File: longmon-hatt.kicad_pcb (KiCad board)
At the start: 2 copper layers, 67 x 35 mm, 4 parts

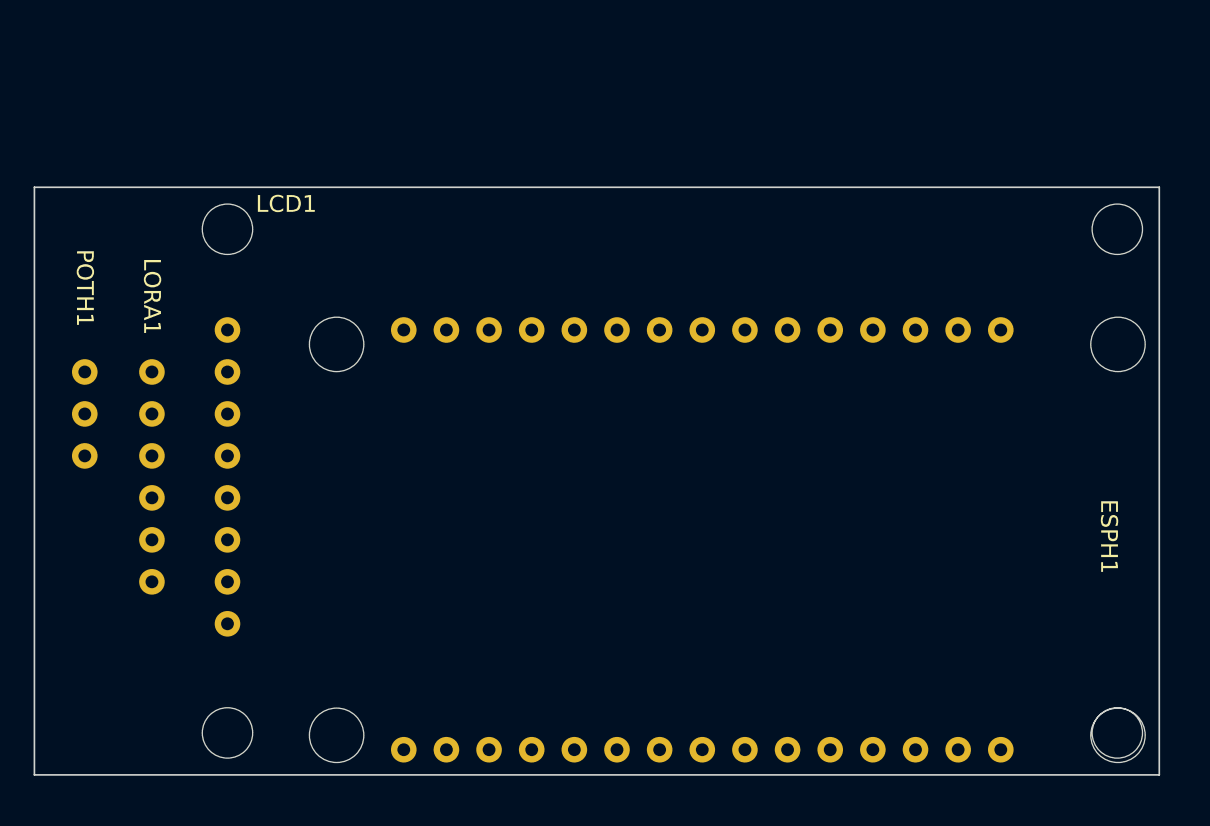
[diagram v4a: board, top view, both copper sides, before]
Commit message: Extend pcb 0.5mm down
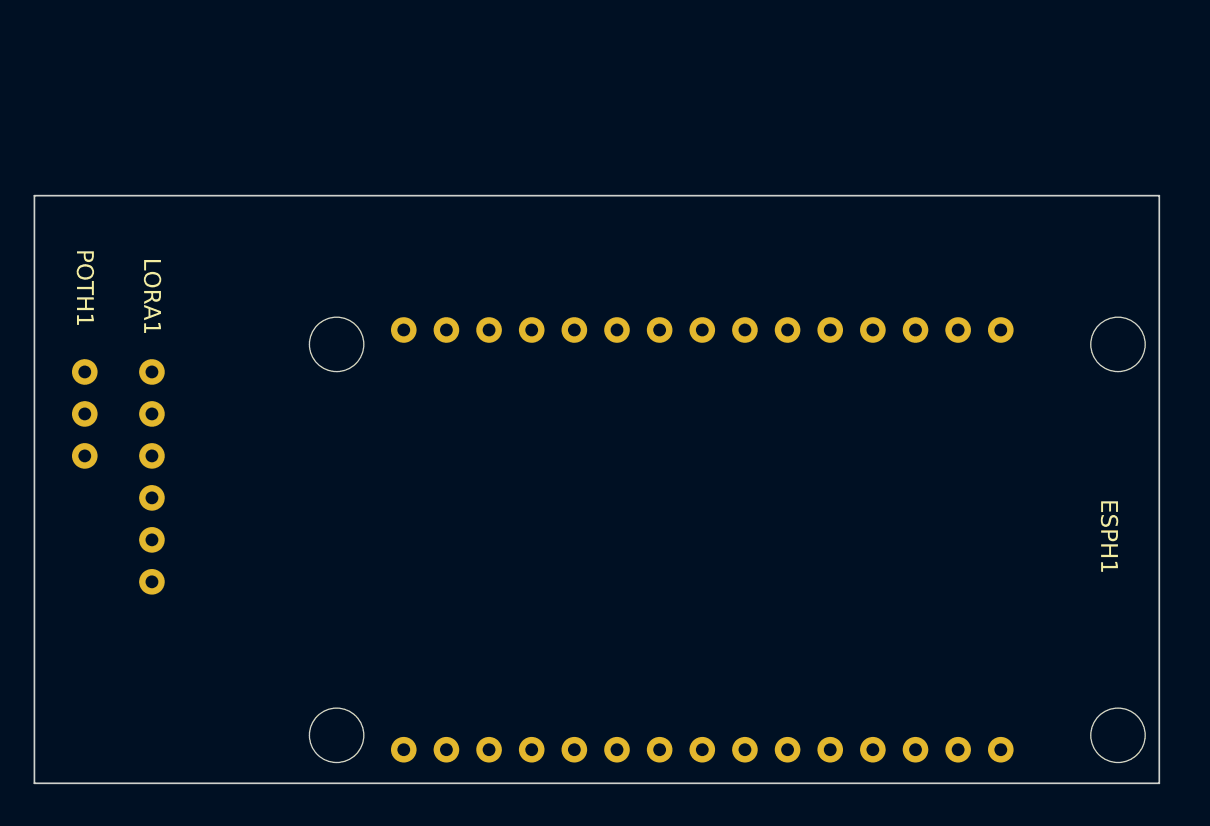
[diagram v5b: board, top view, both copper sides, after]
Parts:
- removed LCD1: ~, ESP:LCD Module

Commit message: Add LCD to PCB
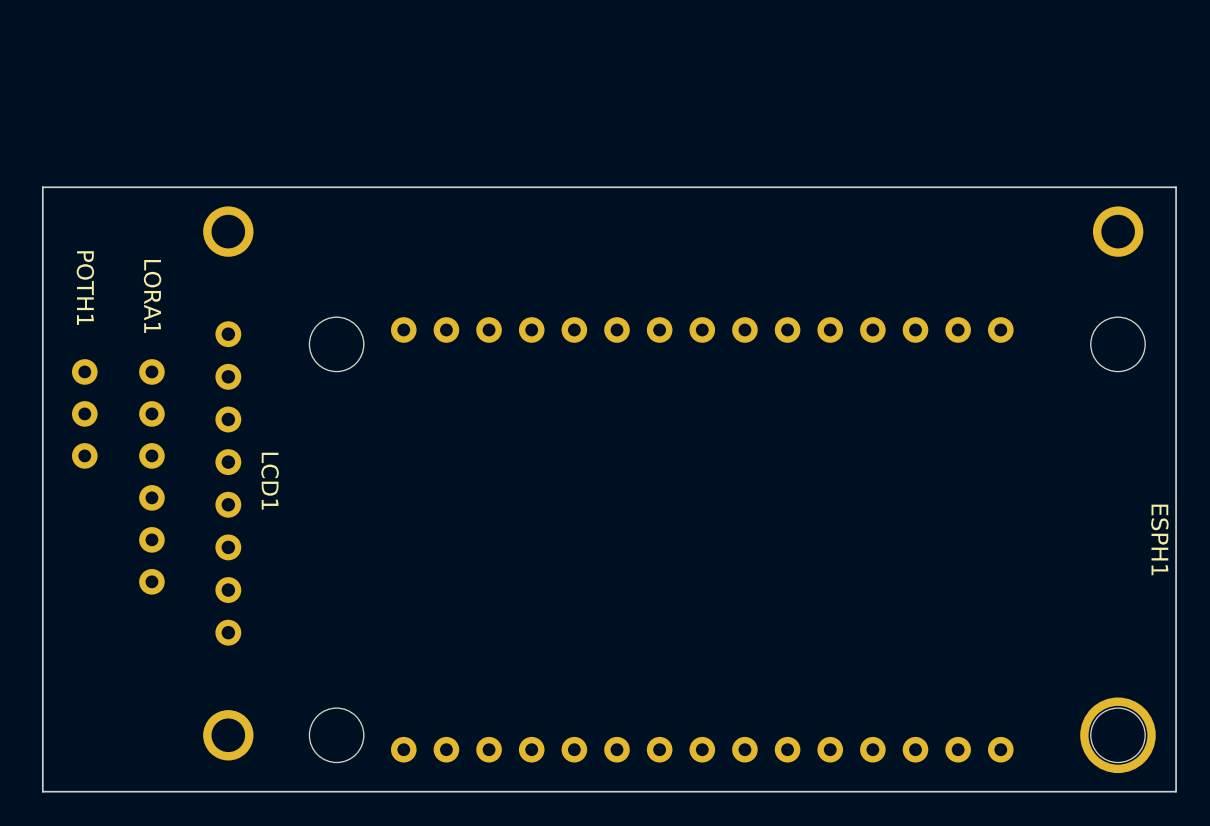
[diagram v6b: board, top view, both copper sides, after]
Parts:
- added LCD1: ~, ESP:LCD Module, F.Cu at (139.6, 81.6)
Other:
- board size 67 x 35 mm -> 67.5 x 36 mm

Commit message: Remove LCD 4th mounting hole, silkscreen thickness to 0.153mm
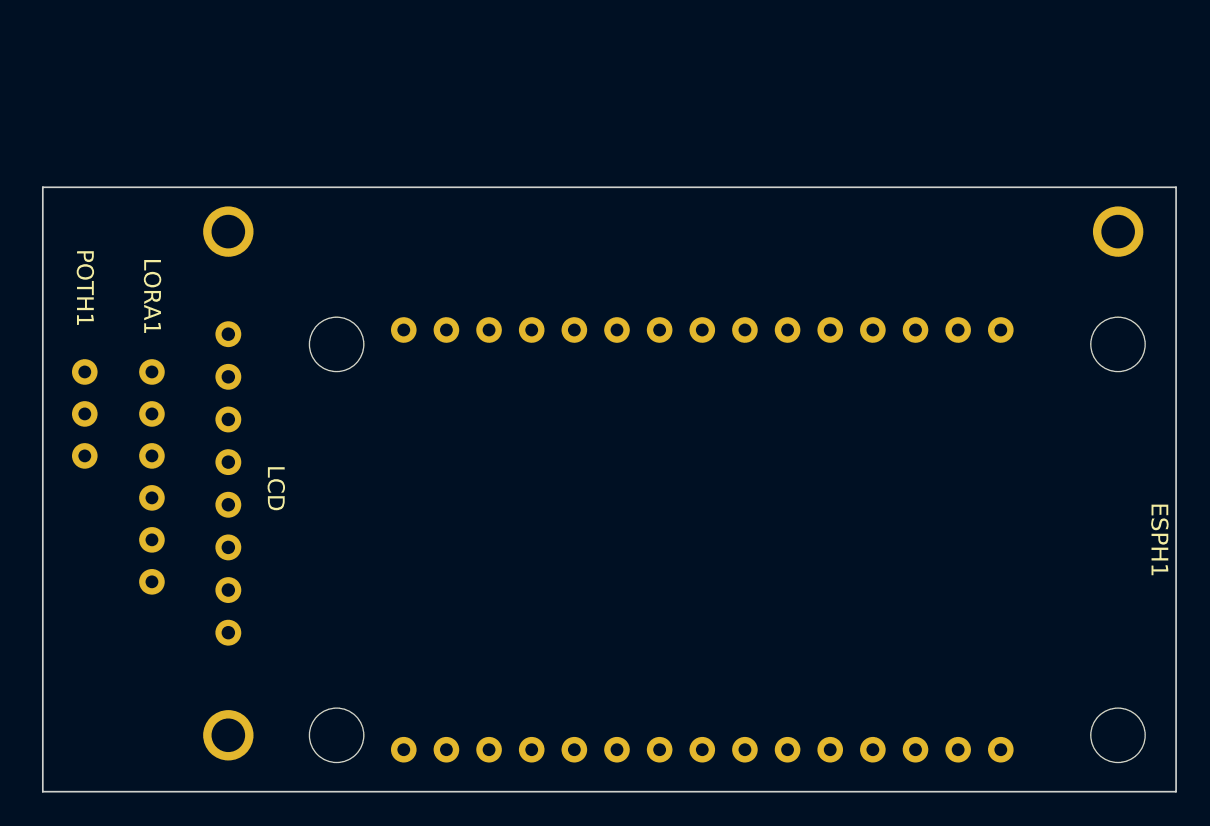
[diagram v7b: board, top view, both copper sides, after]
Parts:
- removed LCD1: ~, ESP:LCD Module
- added LCD: LCD Module, ESP:LCD Module, F.Cu at (139.6, 81.6)
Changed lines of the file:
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@@
     (attr through_hole)
     (fp_text reference "ESPH1" (at 12.5 45 270 unlocked) (layer "F.SilkS")
-        (effects (font (size 1 1) (thickness 0.1)))
+        (effects (font (size 1 1) (thickness 0.153)))
     )
     (fp_text value "~" (at 12.7 0 90 unlocked) (layer "F.Fab") hide
@@
     (property "Sim.Enable" "0")
     (attr through_hole)
-    (fp_text reference "LORA1" (at 0 -4.5 -90 unlocked) (layer "F.SilkS")
-        (effects (font (size 1 1) (thickness 0.1)))
+    (fp_text reference "LORA1" (at 0 -4.5 270 unlocked) (layer "F.SilkS")
+        (effects (font (size 1 1) (thickness 0.153)))
     )
     (fp_text value "~" (at 12.5 -5 unlocked) (layer "F.Fab") hide
@@
       (net 1 "Net-(LCD1-VCC)") (pinfunction "VDD") (pintype "power_in"))
   )
-  (footprint "ESP:POT Header" (layer "F.Cu")
-    (at 131 90)
-    (property "Sheetfile" "longmon-hatt.kicad_sch")
-    (property "Sheetname" "")
-    (property "Sim.Enable" "0")
-    (attr through_hole)
-    (fp_text reference "POTH1" (at 0 -5 -90 unlocked) (layer "F.SilkS")
-        (effects (font (size 1 1) (thickness 0.1)))
-    )
-    (fp_text value "~" (at 7.5 1.5 unlocked) (layer "F.Fab") hide
-        (effects (font (size 1 1) (thickness 0.15)))
-    )
-    (fp_text user "${REFERENCE}" (at 7.5 3 unlocked) (layer "F.Fab") hide
-        (effects (font (size 1 1) (thickness 0.15)))
-    )
-    (pad "DIV" thru_hole circle (at 0 2.5) (size 1.524 1.524) (drill 0.762) (layers "*.Cu" "*.Mask")
-      (net 5 "Net-(ESPH1-D34)") (pinfunction "DIV") (pintype "output"))
-    (pad "GND" thru_hole circle (at 0 5) (size 1.524 1.524) (drill 0.762) (layers "*.Cu" "*.Mask")
-      (net 28 "Net-(LCD1-GND)") (pinfunction "GND") (pintype "power_in"))
-    (pad "VCC" thru_hole circle (at 0 0) (size 1.524 1.524) (drill 0.762) (layers "*.Cu" "*.Mask")
-      (net 1 "Net-(LCD1-VCC)") (pinfunction "VCC") (pintype "power_in"))
-  )
   (footprint "ESP:LCD Module" (layer "F.Cu")
     (at 139.55 81.64)
-    (property "Sheetfile" "longmon-hatt.kicad_sch")
-    (property "Sheetname" "")
-    (property "Sim.Enable" "0")
     (attr through_hole)
-    (fp_text reference "LCD1" (at 2.45 14.86 -90 unlocked) (layer "F.SilkS")
-        (effects (font (size 1 1) (thickness 0.1)))
+    (fp_text reference "LCD" (at 2.82 15.29 -90 unlocked) (layer "F.SilkS")
+        (effects (font (size 1 1) (thickness 0.153)))
     )
-    (fp_text value "~" (at 22.86 -9.12 unlocked) (layer "F.Fab") hide
+    (fp_text value "LCD Module" (at 22.86 -9.12 unlocked) (layer "F.Fab") hide
         (effects (font (size 1 1) (thickness 0.15)))
     )
@@
       )
     )
-    (fp_text user "${REFERENCE}" (at 2.45 14.86 -90 unlocked) (layer "F.Fab")
+    (fp_text user "${REFERENCE}" (at 2.82 15.29 -90 unlocked) (layer "F.Fab")
         (effects (font (size 1 1) (thickness 0.15)))
     )
     (pad "" np_thru_hole circle (at 0 0) (size 3 3) (drill 2) (layers "F&B.Cu" "*.Mask"))
     (pad "" np_thru_hole circle (at 0 30) (size 3 3) (drill 2) (layers "F&B.Cu" "*.Mask"))
-    (pad "" np_thru_hole circle (at 52.99 30) (size 4.5 4.5) (drill 3.5) (layers "F&B.Cu" "*.Mask"))
     (pad "" np_thru_hole circle (at 53 0) (size 3 3) (drill 2) (layers "F&B.Cu" "*.Mask"))
-    (pad "1" thru_hole circle (at 0 6.11) (size 1.54 1.54) (drill 0.8) (layers "*.Cu" "*.Mask")
-      (net 1 "Net-(LCD1-VCC)") (pinfunction "VCC") (pintype "power_in"))
-    (pad "2" thru_hole circle (at 0 8.65) (size 1.54 1.54) (drill 0.8) (layers "*.Cu" "*.Mask")
+    (pad "1" thru_hole circle (at 0 6.11) (size 1.54 1.54) (drill 0.8) (layers "*.Cu" "*.Mask"))
+    (pad "2" thru_hole circle (at 0 8.65) (size 1.54 1.54) (drill 0.8) (layers "*.Cu" "*.Mask"))
+    (pad "3" thru_hole circle (at 0 11.19) (size 1.54 1.54) (drill 0.8) (layers "*.Cu" "*.Mask"))
+    (pad "4" thru_hole circle (at 0 13.73) (size 1.54 1.54) (drill 0.8) (layers "*.Cu" "*.Mask"))
+    (pad "5" thru_hole circle (at 0 16.27) (size 1.54 1.54) (drill 0.8) (layers "*.Cu" "*.Mask"))
+    (pad "6" thru_hole circle (at 0 18.81) (size 1.54 1.54) (drill 0.8) (layers "*.Cu" "*.Mask"))
+    (pad "7" thru_hole circle (at 0 21.35) (size 1.54 1.54) (drill 0.8) (layers "*.Cu" "*.Mask"))
+    (pad "8" thru_hole circle (at 0 23.89) (size 1.54 1.54) (drill 0.8) (layers "*.Cu" "*.Mask"))
+  )
+  (footprint "ESP:POT Header" (layer "F.Cu")
+    (at 131 90)
+    (property "Sheetfile" "longmon-hatt.kicad_sch")
+    (property "Sheetname" "")
+    (property "Sim.Enable" "0")
+    (attr through_hole)
+    (fp_text reference "POTH1" (at 0 -5 270 unlocked) (layer "F.SilkS")
+        (effects (font (size 1 1) (thickness 0.153)))
+    )
+    (fp_text value "~" (at 7.5 1.5 unlocked) (layer "F.Fab") hide
+        (effects (font (size 1 1) (thickness 0.15)))
+    )
+    (fp_text user "${REFERENCE}" (at 7.5 3 unlocked) (layer "F.Fab") hide
+        (effects (font (size 1 1) (thickness 0.15)))
+    )
+    (pad "DIV" thru_hole circle (at 0 2.5) (size 1.524 1.524) (drill 0.762) (layers "*.Cu" "*.Mask")
+      (net 5 "Net-(ESPH1-D34)") (pinfunction "DIV") (pintype "output"))
+    (pad "GND" thru_hole circle (at 0 5) (size 1.524 1.524) (drill 0.762) (layers "*.Cu" "*.Mask")
       (net 28 "Net-(LCD1-GND)") (pinfunction "GND") (pintype "power_in"))
-    (pad "3" thru_hole circle (at 0 11.19) (size 1.54 1.54) (drill 0.8) (layers "*.Cu" "*.Mask")
-      (net 22 "Net-(ESPH1-D23)") (pinfunction "DIN") (pintype "input"))
-    (pad "4" thru_hole circle (at 0 13.73) (size 1.54 1.54) (drill 0.8) (layers "*.Cu" "*.Mask")
-      (net 21 "Net-(ESPH1-D18)") (pinfunction "CLK") (pintype "input"))
-    (pad "5" thru_hole circle (at 0 16.27) (size 1.54 1.54) (drill 0.8) (layers "*.Cu" "*.Mask")
-      (net 20 "Net-(ESPH1-D5)") (pinfunction "CS") (pintype "input"))
-    (pad "6" thru_hole circle (at 0 18.81) (size 1.54 1.54) (drill 0.8) (layers "*.Cu" "*.Mask")
-      (net 23 "Net-(ESPH1-D19)") (pinfunction "DC") (pintype "input"))
-    (pad "7" thru_hole circle (at 0 21.35) (size 1.54 1.54) (drill 0.8) (layers "*.Cu" "*.Mask")
-      (net 17 "Net-(ESPH1-D4)") (pinfunction "RST") (pintype "input"))
-    (pad "8" thru_hole circle (at 0 23.89) (size 1.54 1.54) (drill 0.8) (layers "*.Cu" "*.Mask")
-      (net 27 "Net-(ESPH1-D21)") (pinfunction "BL") (pintype "input"))
+    (pad "VCC" thru_hole circle (at 0 0) (size 1.524 1.524) (drill 0.762) (layers "*.Cu" "*.Mask")
+      (net 1 "Net-(LCD1-VCC)") (pinfunction "VCC") (pintype "power_in"))
   )
   (gr_rect (start 128.5 79) (end 196 115)

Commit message: Autoroute traces
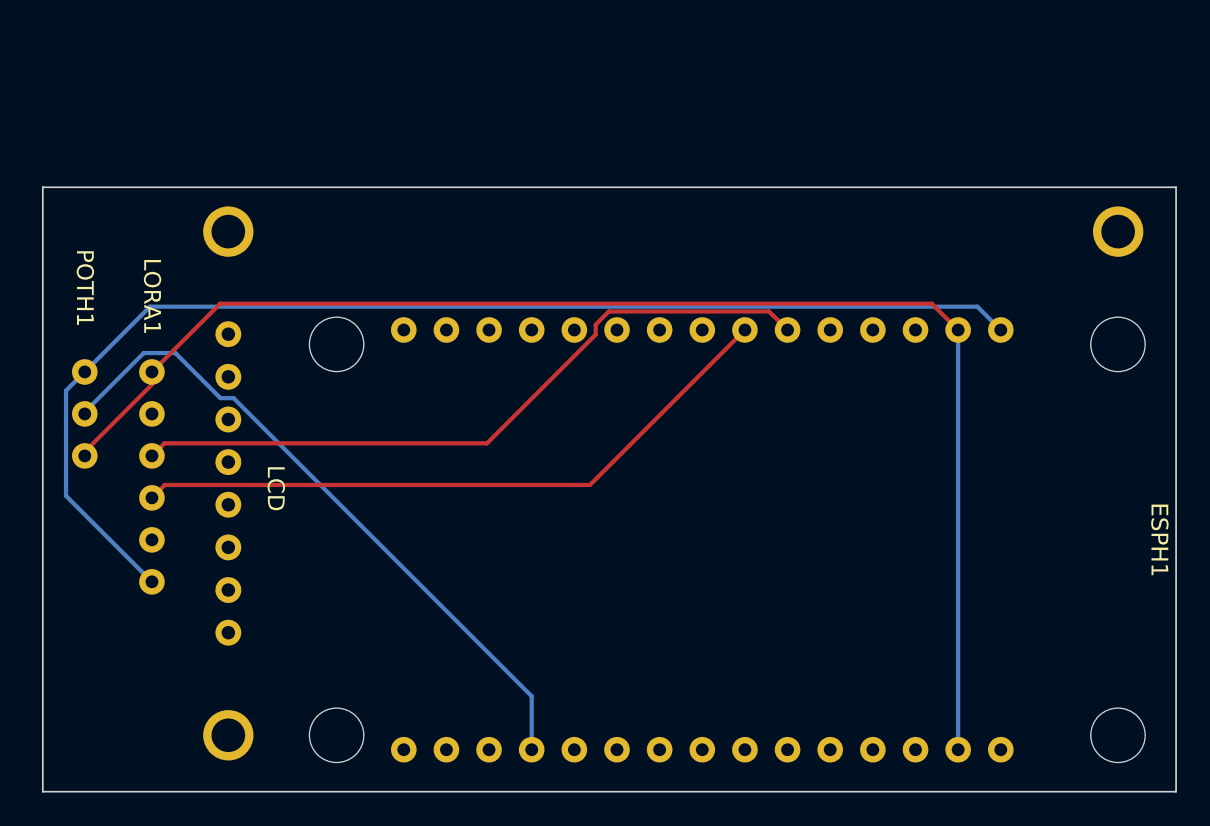
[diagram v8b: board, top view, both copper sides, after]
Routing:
- net Net-(LCD1-GND): track 0.00 -> 82.0 mm
- net Net-(LCD1-VCC): track 0.00 -> 71.8 mm
- net Net-(ESPH1-RX2): track 0.00 -> 42.2 mm
- net Net-(ESPH1-D34): track 0.00 -> 39.8 mm
- net Net-(ESPH1-TX2): track 0.00 -> 39.5 mm
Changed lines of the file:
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@@
   (gr_rect (start 128.5 79) (end 196 115)
     (stroke (width 0.1) (type default)) (fill none) (layer "Edge.Cuts"))
+  (segment (start 129.8842 97.3842) (end 129.8842 91.1158) (width 0.25) (layer "B.Cu") (net 1))
+  (segment (start 135 102.5) (end 129.8842 97.3842) (width 0.25) (layer "B.Cu") (net 1))
+  (segment (start 131 90) (end 134.8886 86.1114) (width 0.25) (layer "B.Cu") (net 1))
+  (segment (start 129.8842 91.1158) (end 131 90) (width 0.25) (layer "B.Cu") (net 1))
+  (segment (start 184.1714 86.1114) (end 185.56 87.5) (width 0.25) (layer "B.Cu") (net 1))
+  (segment (start 134.8886 86.1114) (end 184.1714 86.1114) (width 0.25) (layer "B.Cu") (net 1))
+  (segment (start 157.62 109.3175) (end 157.62 112.5) (width 0.25) (layer "B.Cu") (net 5))
+  (segment (start 134.514 88.8739) (end 136.3937 88.8739) (width 0.25) (layer "B.Cu") (net 5))
+  (segment (start 139.8625 91.56) (end 157.62 109.3175) (width 0.25) (layer "B.Cu") (net 5))
+  (segment (start 131 92.3879) (end 134.514 88.8739) (width 0.25) (layer "B.Cu") (net 5))
+  (segment (start 139.0798 91.56) (end 139.8625 91.56) (width 0.25) (layer "B.Cu") (net 5))
+  (segment (start 136.3937 88.8739) (end 139.0798 91.56) (width 0.25) (layer "B.Cu") (net 5))
+  (segment (start 131 92.5) (end 131 92.3879) (width 0.25) (layer "B.Cu") (net 5))
+  (segment (start 162.2121 86.3979) (end 171.7557 86.3979) (width 0.25) (layer "F.Cu") (net 18))
+  (segment (start 135.749 94.251) (end 154.9559 94.251) (width 0.25) (layer "F.Cu") (net 18))
+  (segment (start 135 95) (end 135.749 94.251) (width 0.25) (layer "F.Cu") (net 18))
+  (segment (start 171.9791 86.6213) (end 171.9813 86.6213) (width 0.25) (layer "F.Cu") (net 18))
+  (segment (start 161.43 87.18) (end 162.2121 86.3979) (width 0.25) (layer "F.Cu") (net 18))
+  (segment (start 161.43 87.7769) (end 161.43 87.18) (width 0.25) (layer "F.Cu") (net 18))
+  (segment (start 171.7557 86.3979) (end 171.9791 86.6213) (width 0.25) (layer "F.Cu") (net 18))
+  (segment (start 171.9813 86.6213) (end 172.86 87.5) (width 0.25) (layer "F.Cu") (net 18))
+  (segment (start 154.9559 94.251) (end 161.43 87.7769) (width 0.25) (layer "F.Cu") (net 18))
+  (segment (start 135.7684 96.7316) (end 161.0884 96.7316) (width 0.25) (layer "F.Cu") (net 19))
+  (segment (start 135 97.5) (end 135.7684 96.7316) (width 0.25) (layer "F.Cu") (net 19))
+  (segment (start 161.0884 96.7316) (end 170.32 87.5) (width 0.25) (layer "F.Cu") (net 19))
+  (segment (start 139.0639 85.9361) (end 181.4561 85.9361) (width 0.25) (layer "F.Cu") (net 28))
+  (segment (start 131 95) (end 131 94.7509) (width 0.25) (layer "F.Cu") (net 28))
+  (segment (start 181.4561 85.9361) (end 183.02 87.5) (width 0.25) (layer "F.Cu") (net 28))
+  (segment (start 131 94.7509) (end 135 90.7509) (width 0.25) (layer "F.Cu") (net 28))
+  (segment (start 135 90) (end 139.0639 85.9361) (width 0.25) (layer "F.Cu") (net 28))
+  (segment (start 135 90.7509) (end 135 90) (width 0.25) (layer "F.Cu") (net 28))
+  (segment (start 183.02 87.5) (end 183.02 112.5) (width 0.25) (layer "B.Cu") (net 28))
 )
